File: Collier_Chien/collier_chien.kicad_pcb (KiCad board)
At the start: 2 copper layers, 60 x 30 mm, 47 parts, among them J10 P-MFC, J19 Conn_01x02_Socket, J20 ANTENNE 868MHz / 50 ohms, J21 UART2 / RUI3, J22 SWD, J3 Conn_01x02_Pin, J4 Conn_01x02_Pin, SW1 RESET, U1 RAK3172(H) / EU868, U2 BQ25570, U3 LIS2HH12

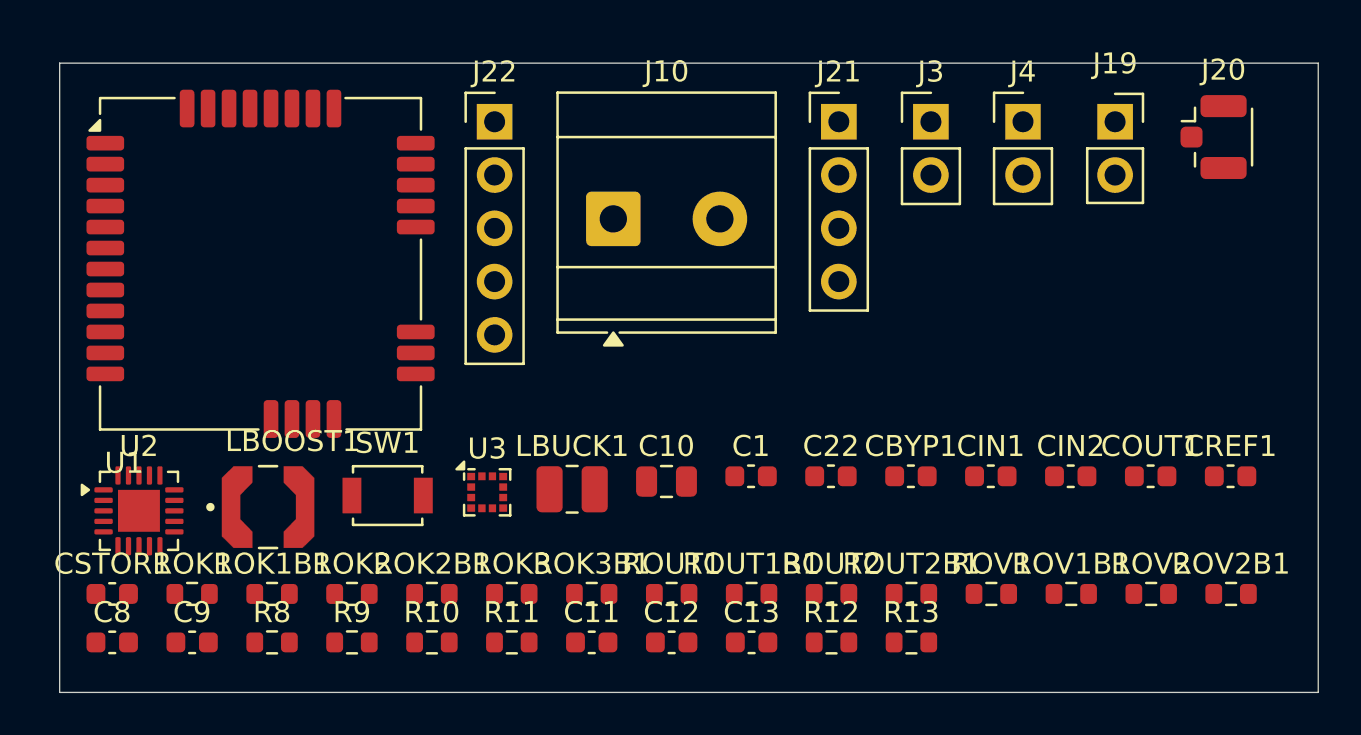
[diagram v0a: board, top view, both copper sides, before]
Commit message: Route le collier 60x30 sur deux couches avec plan de masse et retour RF protege
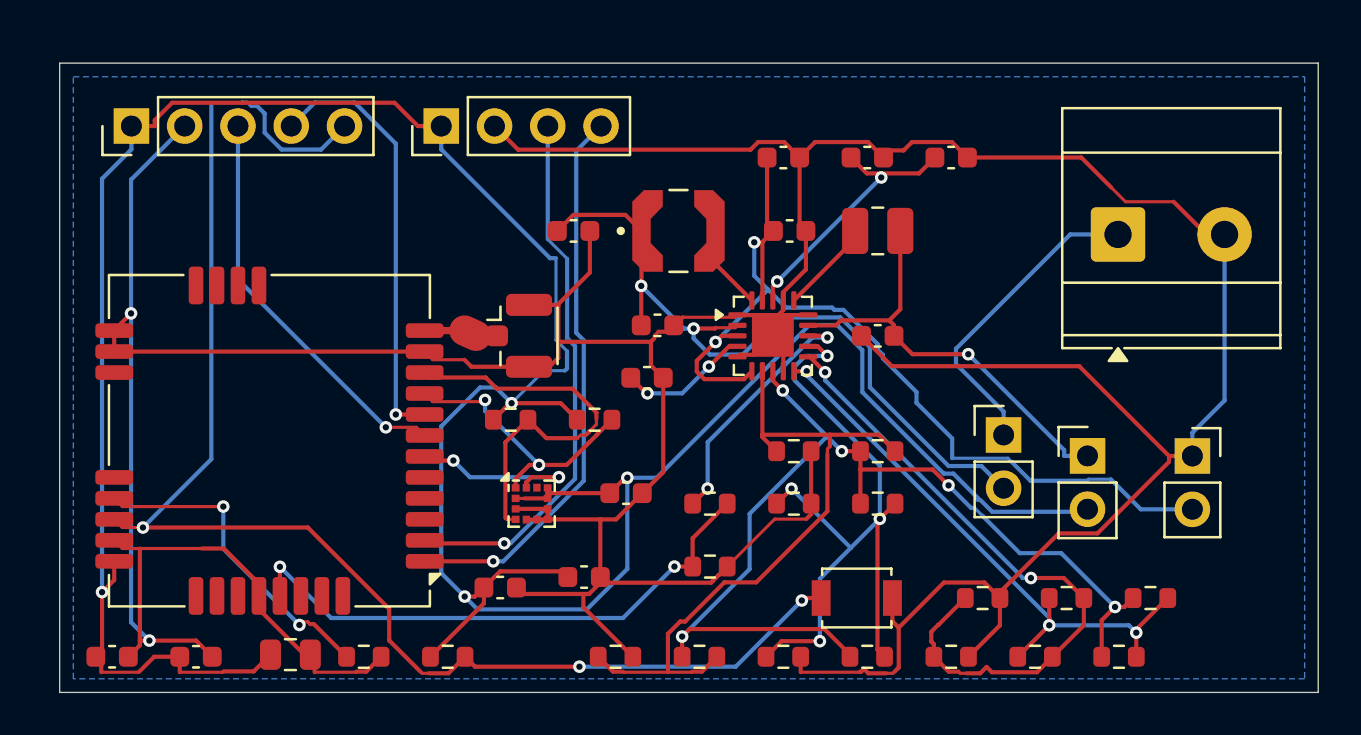
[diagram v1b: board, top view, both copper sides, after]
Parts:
- moved CSTOR1 38.2 mm to (134.5, 104.5)
- moved ROK1 37.7 mm to (144.0, 125.5)
- moved J20 34.4 mm to (122.4, 113.0)
- moved ROK2 34.1 mm to (148.0, 125.5)
- moved ROK1B1 32.5 mm to (142.5, 128.3)
- moved U2 31.4 mm to (134.0, 113.0)
- moved ROK3 30.4 mm to (152.0, 125.5)
- moved ROK2B1 28.9 mm to (146.5, 128.3)
- moved CREF1 28.2 mm to (128.0, 115.0)
- moved ROV2B1 25.5 mm to (130.5, 128.3)
- moved ROK3B1 25.3 mm to (150.5, 128.3)
- moved J10 24.1 mm to (150.5, 108.2)
- moved LBOOST1 23.6 mm to (129.5, 108.0)
- moved CIN1 23.1 mm to (124.5, 108.0)
- moved SW1 22.9 mm to (138.0, 125.5)
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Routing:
- net 'EN: track 0.00 -> 248.9 mm, vias 0 -> 2
- net PWR: track 0.00 -> 148.2 mm, vias 0 -> 4
- net /Traitement / RAK3172/NRST: track 0.00 -> 69.4 mm, vias 0 -> 3
- net /Alimentation / BQ25570/VRDIV: track 0.00 -> 49.2 mm, vias 0 -> 5
- net VOUT_EN: track 0.00 -> 45.2 mm, vias 0 -> 2
- net Net-(J4-Pin_2): track 0.00 -> 35.4 mm, vias 0 -> 2
- net Net-(U2-VOUT_SET): track 0.00 -> 34.5 mm, vias 0 -> 4
- net Net-(U2-VBAT_OV): track 0.00 -> 32.5 mm
- net Net-(U2-OK_PROG): track 0.00 -> 31.6 mm, vias 0 -> 2
- net Net-(U2-OK_HYST): track 0.00 -> 28.7 mm, vias 0 -> 3
- net VBAT_OK_3V3: track 0.00 -> 26.8 mm, vias 0 -> 2
- net /Traitement / RAK3172/UART2_RX: track 0.00 -> 26.7 mm, vias 0 -> 1
- net /Traitement / RAK3172/UART2_TX: track 0.00 -> 25.9 mm, vias 0 -> 1
- net Net-(J3-Pin_1): track 0.00 -> 21.0 mm, vias 0 -> 1
- net /Traitement / RAK3172/SWCLK: track 0.00 -> 20.5 mm, vias 0 -> 1
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- added copper zone on B.Cu, net 'EN
